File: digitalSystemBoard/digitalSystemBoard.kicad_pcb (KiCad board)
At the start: 2 copper layers, 180 x 130 mm, 197 parts, among them J0 Barrel_Jack, J1 USB-B, J10 Conn_02x03_Odd_Even, J11 Conn_02x03_Odd_Even, J12 Conn_01x10_Female, J13 Conn_01x10_Female, J14 Conn_01x10_Female, J15 Conn_01x10_Female, J2 Conn_02x04_Odd_Even, J3 Conn_02x04_Odd_Even, J4 Conn_02x08_Odd_Even, J5 Conn_02x07_Odd_Even, J6 Conn_02x07_Odd_Even, J7 Conn_02x08_Odd_Even, J8 Conn_02x03_Odd_Even, J9 Conn_02x03_Odd_Even, Q0 BC847, Q1 BC847, Q10 BC847, Q11 BC847, Q12 BC847, Q13 BC847, Q14 BC847, Q15 BC847, Q2 BC847, Q3 BC847, Q4 BC847, Q5 BC847, Q6 BC847, Q7 BC847, Q8 BC847, Q9 BC847, SW0 SW_SPDT, SW1 IO_Switch, SW2 IO_Switch, SW3 IO_Switch, SW4 IO_Switch, SW5 IO_Switch, SW6 IO_Switch, SW7 IO_Switch, SW8 IO_Switch, SW9 ButtonFirst, U0 KCSA02-105, U1 KCSA02-105, U10 74HC165, U11 74HC595, U2 74LS47, U3 74LS47, U4 74LS04, U5 Potentiometer, U7 ICSP, U8 74HC165, U9 74HC595

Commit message: Edit some track
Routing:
- net GND: track 1362.4 -> 1355.6 mm
- net /VCC5V: track 1166.8 -> 1168.1 mm
- net /MCU/VCC_2: track 11.5 -> 10.9 mm
- net /MCU/VCC_1: track 8.47 -> 7.92 mm
- net /MCU/VCC_3: track 12.5 -> 11.9 mm

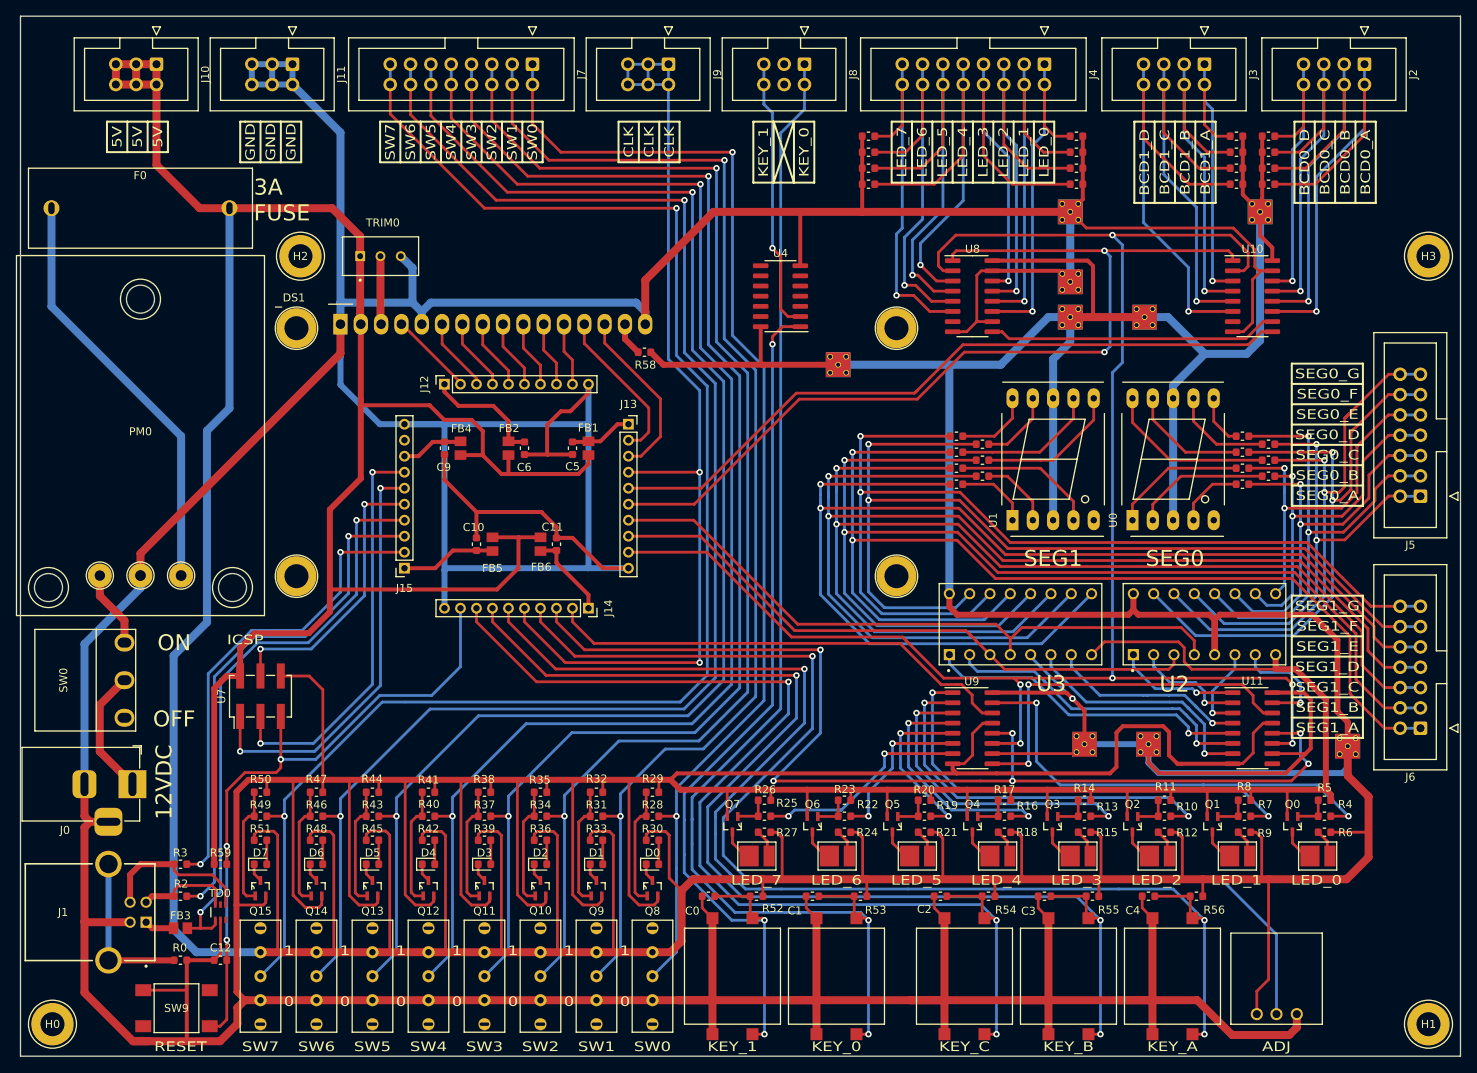
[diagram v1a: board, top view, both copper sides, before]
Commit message: Generate BOM, Gerber and CPL file
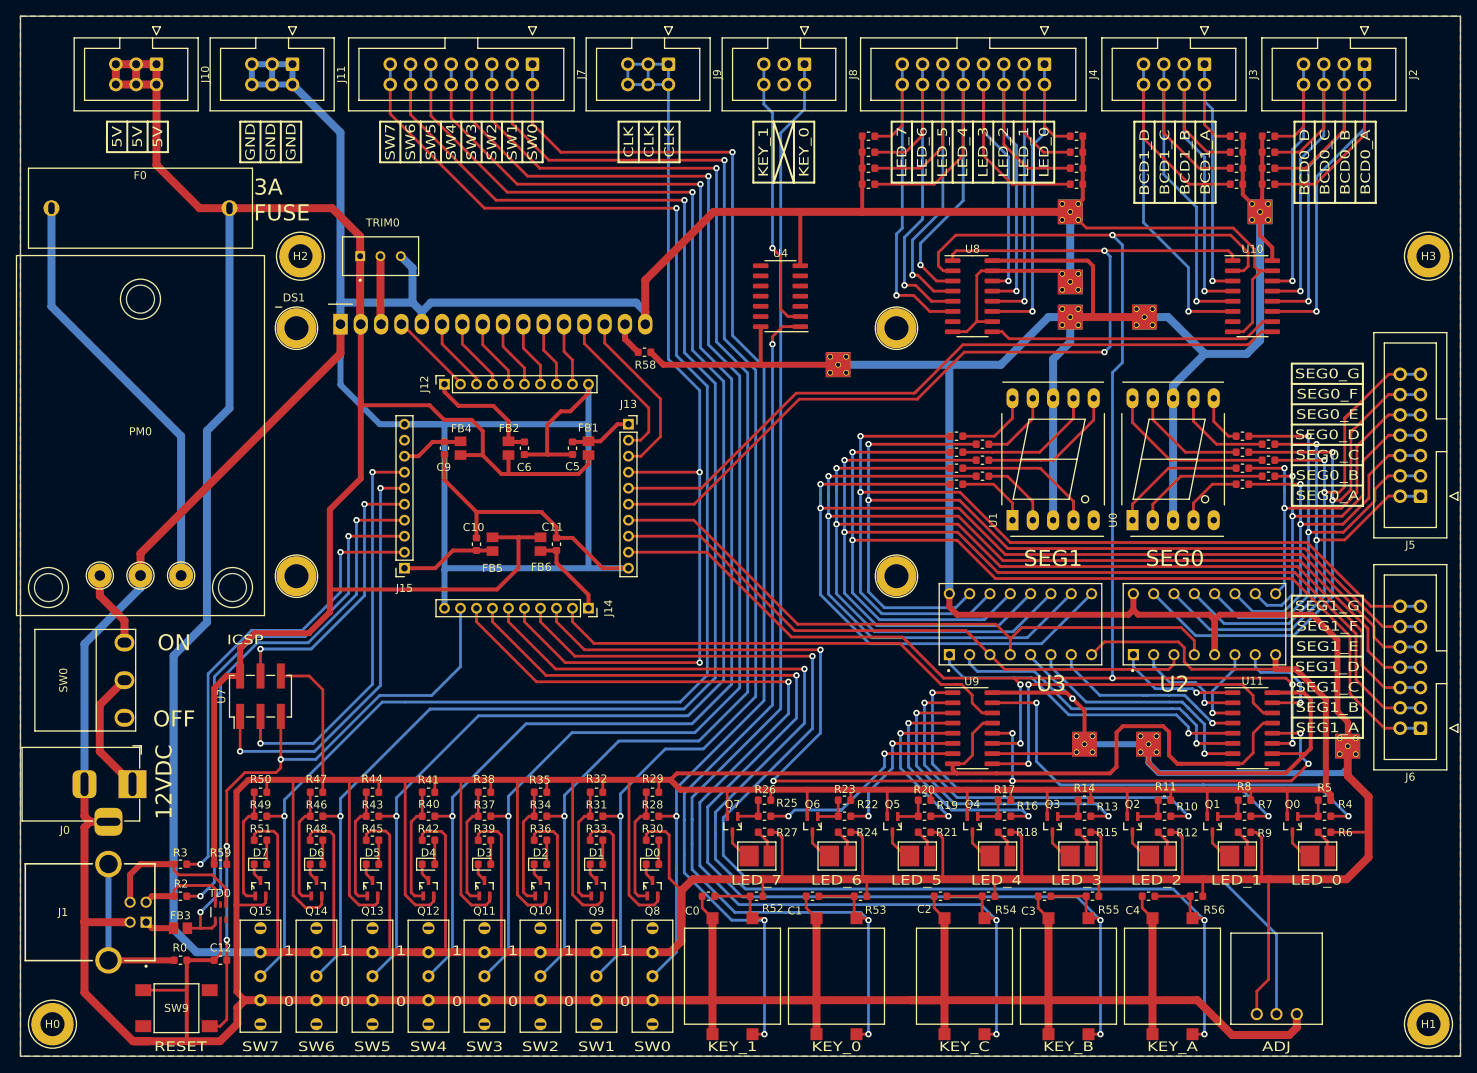
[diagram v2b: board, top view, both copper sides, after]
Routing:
- added copper zone on B.Cu, net GND
- added copper zone on F.Cu, net GND
